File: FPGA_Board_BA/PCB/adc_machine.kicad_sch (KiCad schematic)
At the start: 6 parts, among them J201 PinHeader_03_male, U201 LTC2320-16_LVDS

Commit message: some schematic changes + Misc
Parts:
- removed C201, C202, C203, C204: 10u_1210, WLIB_Capacitor:C_1210, symbol WLIB_C:10u_1210
- removed J201: PinHeader_03_male, Connector_PinHeader_2.54mm:PinHeader_1x03_P2.54mm_Vertical, symbol WLIB_J:PinHeader_03_male
- removed U201: LTC2320-16_LVDS, MYLIB_chips:UKG_52_7mm_8mm, symbol MYLIB_U:LTC2320-16_LVDS
- added C1301, C1302, C1303, C1304: 10u_1210, WLIB_Capacitor:C_1210, symbol WLIB_C:10u_1210
- added U1301: LTC2320-16_LVDS, MYLIB_chips:UKG_52_7mm_8mm, symbol MYLIB_U:LTC2320-16_LVDS
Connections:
- net +5VA: now also U1301.15 (VDD), U1301.21 (VDD), U1301.43 (REFBUFEN), U1301.44 (VDD), U1301.52 (VDD)
- net GND: now also C1301.2, C1302.2, C1303.2, C1304.2, U1301.12 (GND), U1301.18 (GND), U1301.26 (GND), U1301.3 (GND), U1301.32 (GND), U1301.34 (CLKOUT-), U1301.38 (GND), U1301.46 (GND), U1301.49 (GND), U1301.53 (GND), U1301.7 (GND)
- net OVDD: now also U1301.23 (~{SDR}/DDR), U1301.25 (~{CMOS}/LVDS), U1301.31 (OVDD), U1301.37 (OVDD)
- new net: C1303.1, U1301.6 (REFOUT3)
- new net: C1301.1, U1301.22 (REFOUT1)
- new net: C1302.1, U1301.9 (REFOUT2)
- new net: C1304.1, U1301.45 (REFOUT4)
- new net CLK_IN_1: U1301.41 (SCK+)
- new net CLK_OUT_1: U1301.33 (CLKOUT+)
- new net SDO1_1: U1301.27 (SDOA+)
- new net SDO2_1: U1301.28 (SDOA-)
- new net SDO3_1: U1301.29 (SDOB+)
- new net SDO4_1: U1301.30 (SDOB-)
- new net SDO5_1: U1301.35 (SDOC+)
- new net SDO6_1: U1301.36 (SDOC-)
- new net SDO7_1: U1301.39 (SDOD+)
- new net SDO8_1: U1301.40 (SDOD-)
- new net ~{CNV}_1: U1301.24 (~{CNV})
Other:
- note removed: "Buffer for input: LT1819 or Leo circuit Not pseudo-differential!"
- note removed: "PinHeader for decide 1-2: SDR 2-3: DDR"

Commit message: lot of work
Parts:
- added J1301: PinHeader_03_male, Connector_PinHeader_2.54mm:PinHeader_1x03_P2.54mm_Vertical, symbol WLIB_J:PinHeader_03_male
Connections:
- net GND: now also J1301.1 (Pin_1)
- net Diffamp4/Ain-: now reaches U1301.10 (Ain4-)
- net Diffamp4/Ain+: now reaches U1301.11 (Ain4+)
- net Diffamp3/Ain-: now reaches U1301.13 (Ain3-)
- net Diffamp3/Ain+: now reaches U1301.14 (Ain3+)
- net Diffamp2/Ain-: now reaches U1301.16 (Ain2-)
- net Diffamp2/Ain+: now reaches U1301.17 (Ain2+)
- net Diffamp1/Ain-: now reaches U1301.19 (Ain1-)
- net Diffamp1/Ain+: now reaches U1301.20 (Ain1+)
- net OVDD: no longer names the net of U1301.23 (~{SDR}/DDR), U1301.25 (~{CMOS}/LVDS)
- net OVDD: now also J1301.2 (Pin_2); no longer U1301.31 (OVDD), U1301.37 (OVDD)
- new net +1V8: J1301.3 (Pin_3), U1301.31 (OVDD), U1301.37 (OVDD)
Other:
- added sheet Diffamp1 (diffamp_adc.kicad_sch)
- added sheet Diffamp2 (diffamp_adc.kicad_sch)
- added sheet Diffamp3 (diffamp_adc.kicad_sch)
- added sheet Diffamp4 (diffamp_adc.kicad_sch)
- added sheet Diffamp5 (diffamp_adc.kicad_sch)
- added sheet Diffamp6 (diffamp_adc.kicad_sch)
- added sheet Diffamp7 (diffamp_adc.kicad_sch)
- added sheet Diffamp8 (diffamp_adc.kicad_sch)
- note added: "PinHeader for decide 1-2: SDR 2-3: DDR"
- moved on the sheet: C1301, C1302, C1303, C1304, U1301

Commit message: work
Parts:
- removed U1301: LTC2320-16_LVDS, MYLIB_chips:UKG_52_7mm_8mm, symbol MYLIB_U:LTC2320-16_LVDS
- added C57, C58, C67: 1u_0603, WLIB_Capacitor:C_0603, symbol WLIB_C:1u_0603
- added C59, C60, C61, C62, C63, C64, C65, C66: 100n_0603, WLIB_Capacitor:C_0603, symbol WLIB_C:100n_0603
- added Q6: NTR5103NT1G, Package_TO_SOT_SMD:SOT-23_Handsoldering, symbol WLIB_Q:NTR5103NT1G
- added R52: 100R_0603, Resistor_SMD:R_0603_1608Metric, symbol WLIB_R:100R_0603
- added R53, R54: 10k_0603, Resistor_SMD:R_0603_1608Metric, symbol WLIB_R:10k_0603
- added U15: LTC2320-16_CMOS, MYLIB_chips:UKG_52_7mm_8mm, symbol MYLIB_U:LTC2320-16_CMOS
- renumbered C1301 to C68, C1302 to C69, C1303 to C70, C1304 to C71, J1301 to J19
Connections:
- net +1V8: now also C58.1, C60.1, C62.1, C64.1, C66.1, R54.1, U15.31 (OVDD), U15.37 (OVDD)
- net +5VA: now also C57.1, C59.1, C61.1, C63.1, C65.1, U15.15 (VDD), U15.21 (VDD), U15.43 (REFBUFEN), U15.44 (VDD), U15.52 (VDD)
- net CLK_IN_1: now also U15.41 (SCK)
- net CLK_OUT_1: now also U15.33 (CLKOUT+)
- net Diffamp1/Ain+: now also U15.20 (Ain1+)
- net Diffamp1/Ain-: now also U15.19 (Ain1-)
- net Diffamp2/Ain+: now also U15.17 (Ain2+)
- net Diffamp2/Ain-: now also U15.16 (Ain2-)
- net Diffamp3/Ain+: now also U15.14 (Ain3+)
- net Diffamp3/Ain-: now also U15.13 (Ain3-)
- net Diffamp4/Ain+: now also U15.11 (Ain4+)
- net Diffamp4/Ain-: now also U15.10 (Ain4-)
- net GND: now also C57.2, C58.2, C59.2, C60.2, C61.2, C62.2, C63.2, C64.2, C65.2, C66.2, C67.2, Q6.2 (S), R53.2, U15.12 (GND), U15.18 (GND), U15.25 (~{CMOS}/LVDS), U15.26 (GND), U15.3 (GND), U15.32 (GND), U15.34 (CLKOUT-), U15.38 (GND), U15.46 (GND), U15.49 (GND), U15.53 (GND), U15.7 (GND)
- net SDO1_1: now also U15.27 (SDO1)
- net SDO2_1: now also U15.28 (SDO2)
- net SDO3_1: now also U15.29 (SDO3)
- net SDO4_1: now also U15.30 (SDO4)
- net SDO5_1: now also U15.35 (SDO5)
- net SDO6_1: now also U15.36 (SDO6)
- net SDO7_1: now also U15.39 (SDO7)
- net SDO8_1: now also U15.40 (SDO8)
- net at C70.1: now also U15.6 (REFOUT3)
- net at C68.1: now also U15.22 (REFOUT1)
- net at C69.1: now also U15.9 (REFOUT2)
- net at J19.2 (Pin_2): now also U15.23 (~{SDR}/DDR)
- net at C71.1: now also U15.45 (REFOUT4)
- new net: Q6.1 (G), R52.2, R53.1
- new net: C67.1, U15.8 (REF)
- new net CNV_1: R52.1
- new net ~{CNV}: Q6.3 (D), R54.2, U15.24 (~{CNV})
- no-connect marks 1 -> 0
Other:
- moved on the sheet: C68, C69, C70, C71, J19

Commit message: 18.11 Bib Session
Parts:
- removed Q6: NTR5103NT1G, Package_TO_SOT_SMD:SOT-23_Handsoldering, symbol WLIB_Q:NTR5103NT1G
- removed R52: 100R_0603, Resistor_SMD:R_0603_1608Metric, symbol WLIB_R:100R_0603
- removed R53, R54: 10k_0603, Resistor_SMD:R_0603_1608Metric, symbol WLIB_R:10k_0603
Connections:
- net CLK_IN_1: no longer U15.41 (SCK)
- net ~{CNV} renamed Level Shift for DIO/B2
- new net Level Shift for DIO/B1: U15.41 (SCK)
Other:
- added sheet Level Shift for DIO (ls_for_dio.kicad_sch)

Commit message: 22.11
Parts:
- renumbered C57 to C58, C58 to C59, C59 to C60, C60 to C61, C61 to C62, C62 to C63, C63 to C64, C64 to C65, C65 to C66, C66 to C67, C67 to C68, C68 to C69, C69 to C70, C70 to C71, C71 to C72, U15 to U11
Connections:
- net Diffamp5/Ain+: now also U11.5 (Ain5+)
- net Diffamp5/Ain-: now also U11.4 (Ain5-)
- net Diffamp6/Ain+: now also U11.2 (Ain6+)
- net Diffamp6/Ain-: now also U11.1 (Ain6-)
- net Diffamp7/Ain+: now also U11.51 (Ain7+)
- net Diffamp7/Ain-: now also U11.50 (Ain7-)
- net Diffamp8/Ain+: now also U11.48 (Ain8+)
- net Diffamp8/Ain-: now also U11.47 (Ain8-)
- net REFOUT_1: now reaches C68.1, U11.8 (REF)

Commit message: exported stuff
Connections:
- net REFOUT_1 renamed REFOUT_M
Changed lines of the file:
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@@
+		)
+	)
+	(global_label "REFOUT_M"
+		(shape bidirectional)
+		(at 107.95 114.3 180)
+		(fields_autoplaced yes)
+		(effects
+			(font
+				(size 1.27 1.27)
+			)
+			(justify right)
+		)
+		(property "Intersheetrefs" "${INTERSHEET_REFS}"
+			(at 94.2983 114.3 0)
+			(effects
+				(font
+					(size 1.27 1.27)
+				)
+				(justify right)
+				(hide yes)
+			)
 		)
 	)
@@
 		(dnp no)
 		(fields_autoplaced yes)
-		(property "Reference" "#PWR086"
+		(property "Reference" "#PWR091"
 			(at 52.07 133.35 0)
 			(effects
@@
 			(project "FPGA_Board_BA"
 				(path "/fd7503bc-e7fc-4766-b224-3d1c3d7de5ff/61f82991-823e-4c29-9a78-9b2ec5b110b2"
-					(reference "#PWR086")
+					(reference "#PWR091")
 					(unit 1)
 				)
@@
 		(dnp no)
 		(fields_autoplaced yes)
-		(property "Reference" "#PWR093"
+		(property "Reference" "#PWR099"
 			(at 193.04 45.72 0)
 			(effects
@@
 			(project "FPGA_Board_BA"
 				(path "/fd7503bc-e7fc-4766-b224-3d1c3d7de5ff/61f82991-823e-4c29-9a78-9b2ec5b110b2"
-					(reference "#PWR093")
+					(reference "#PWR099")
 					(unit 1)
 				)
@@
 		(dnp no)
 		(fields_autoplaced yes)
-		(property "Reference" "#PWR087"
+		(property "Reference" "#PWR092"
 			(at 54.61 148.59 0)
 			(effects
@@
 			(project "FPGA_Board_BA"
 				(path "/fd7503bc-e7fc-4766-b224-3d1c3d7de5ff/61f82991-823e-4c29-9a78-9b2ec5b110b2"
-					(reference "#PWR087")
+					(reference "#PWR092")
 					(unit 1)
 				)
@@
 		(dnp no)
 		(fields_autoplaced yes)
-		(property "Reference" "#PWR091"
+		(property "Reference" "#PWR097"
 			(at 182.88 45.72 0)
 			(effects
@@
 			(project ""
 				(path "/fd7503bc-e7fc-4766-b224-3d1c3d7de5ff/61f82991-823e-4c29-9a78-9b2ec5b110b2"
-					(reference "#PWR091")
+					(reference "#PWR097")
 					(unit 1)
 				)
@@
 		(dnp no)
 		(fields_autoplaced yes)
-		(property "Reference" "#PWR089"
+		(property "Reference" "#PWR095"
 			(at 134.62 55.88 0)
 			(effects
@@
 			(project "FPGA_Board_BA"
 				(path "/fd7503bc-e7fc-4766-b224-3d1c3d7de5ff/61f82991-823e-4c29-9a78-9b2ec5b110b2"
-					(reference "#PWR089")
+					(reference "#PWR095")
 					(unit 1)
 				)
@@
 		(dnp no)
 		(fields_autoplaced yes)
-		(property "Reference" "#PWR090"
+		(property "Reference" "#PWR096"
 			(at 140.97 148.59 0)
 			(effects
@@
 			(project "FPGA_Board_BA"
 				(path "/fd7503bc-e7fc-4766-b224-3d1c3d7de5ff/61f82991-823e-4c29-9a78-9b2ec5b110b2"
-					(reference "#PWR090")
+					(reference "#PWR096")
 					(unit 1)
 				)
@@
 		(dnp no)
 		(fields_autoplaced yes)
-		(property "Reference" "#PWR088"
+		(property "Reference" "#PWR093"
 			(at 54.61 168.91 0)
 			(effects
@@
 			(project "FPGA_Board_BA"
 				(path "/fd7503bc-e7fc-4766-b224-3d1c3d7de5ff/61f82991-823e-4c29-9a78-9b2ec5b110b2"
-					(reference "#PWR088")
+					(reference "#PWR093")
 					(unit 1)
 				)
@@
 		(dnp no)
 		(fields_autoplaced yes)
-		(property "Reference" "#PWR085"
+		(property "Reference" "#PWR090"
 			(at 52.07 111.76 0)
 			(effects
@@
 			(project "FPGA_Board_BA"
 				(path "/fd7503bc-e7fc-4766-b224-3d1c3d7de5ff/61f82991-823e-4c29-9a78-9b2ec5b110b2"
-					(reference "#PWR085")
+					(reference "#PWR090")
 					(unit 1)
 				)
@@
 	)
 	(symbol
-		(lib_id "power:+5V")
-		(at 107.95 114.3 90)
-		(unit 1)
-		(exclude_from_sim no)
-		(in_bom yes)
-		(on_board yes)
-		(dnp no)
-		(fields_autoplaced yes)
-		(property "Reference" "#PWR0297"
-			(at 111.76 114.3 0)
-			(effects
-				(font
-					(size 1.27 1.27)
-				)
-				(hide yes)
-			)
-		)
-		(property "Value" "REFOUT_1"
-			(at 104.14 114.2999 90)
-			(effects
-				(font
-					(size 1.27 1.27)
-				)
-				(justify left)
-			)
-		)
-		(property "Footprint" ""
-			(at 107.95 114.3 0)
-			(effects
-				(font
-					(size 1.27 1.27)
-				)
-				(hide yes)
-			)
-		)
-		(property "Datasheet" ""
-			(at 107.95 114.3 0)
-			(effects
-				(font
-					(size 1.27 1.27)
-				)
-				(hide yes)
-			)
-		)
-		(property "Description" "Power symbol creates a global label with name \"REFOUT_1\""
-			(at 107.95 114.3 0)
-			(effects
-				(font
-					(size 1.27 1.27)
-				)
-				(hide yes)
-			)
-		)
-		(pin "1"
-		)
-		(instances
-			(project "FPGA_Board_BA"
-				(path "/fd7503bc-e7fc-4766-b224-3d1c3d7de5ff/61f82991-823e-4c29-9a78-9b2ec5b110b2"
-					(reference "#PWR0297")
-					(unit 1)
-				)
-			)
-		)
-	)
-	(symbol
 		(lib_id "WLIB_C:10u_1210")
 		(at 156.21 129.54 0)
@@
 		(dnp no)
 		(fields_autoplaced yes)
-		(property "Reference" "#PWR092"
+		(property "Reference" "#PWR098"
 			(at 187.96 143.51 0)
 			(effects
@@
 			(project "FPGA_Board_BA"
 				(path "/fd7503bc-e7fc-4766-b224-3d1c3d7de5ff/61f82991-823e-4c29-9a78-9b2ec5b110b2"
-					(reference "#PWR092")
-					(unit 1)
-				)
+					(reference "#PWR098")
+					(unit 1)
+				)

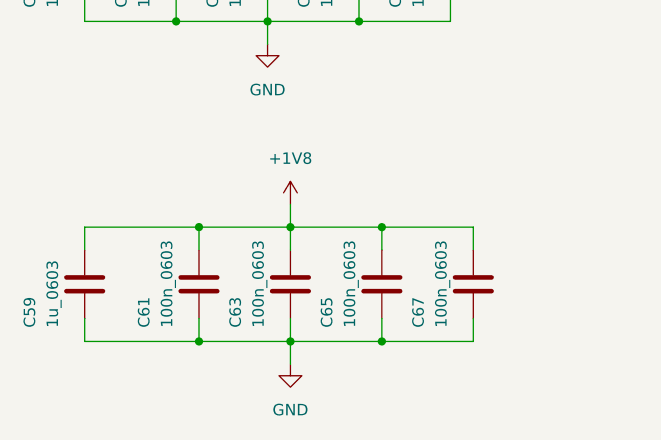
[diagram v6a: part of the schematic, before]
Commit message: layout of islands is ready
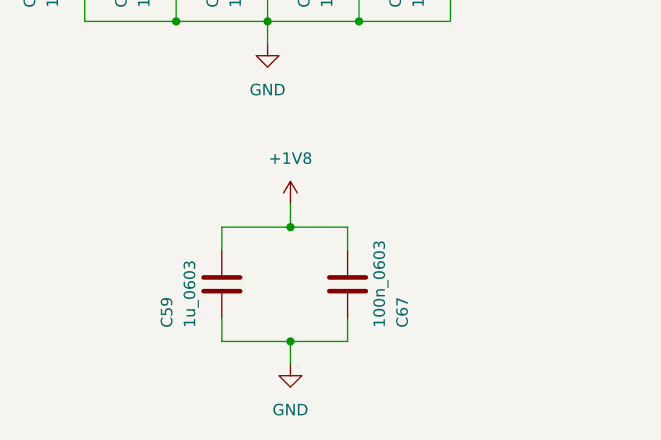
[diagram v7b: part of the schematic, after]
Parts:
- removed C61, C63, C65: 100n_0603, WLIB_Capacitor:C_0603, symbol WLIB_C:100n_0603
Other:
- moved on the sheet: C59, C67

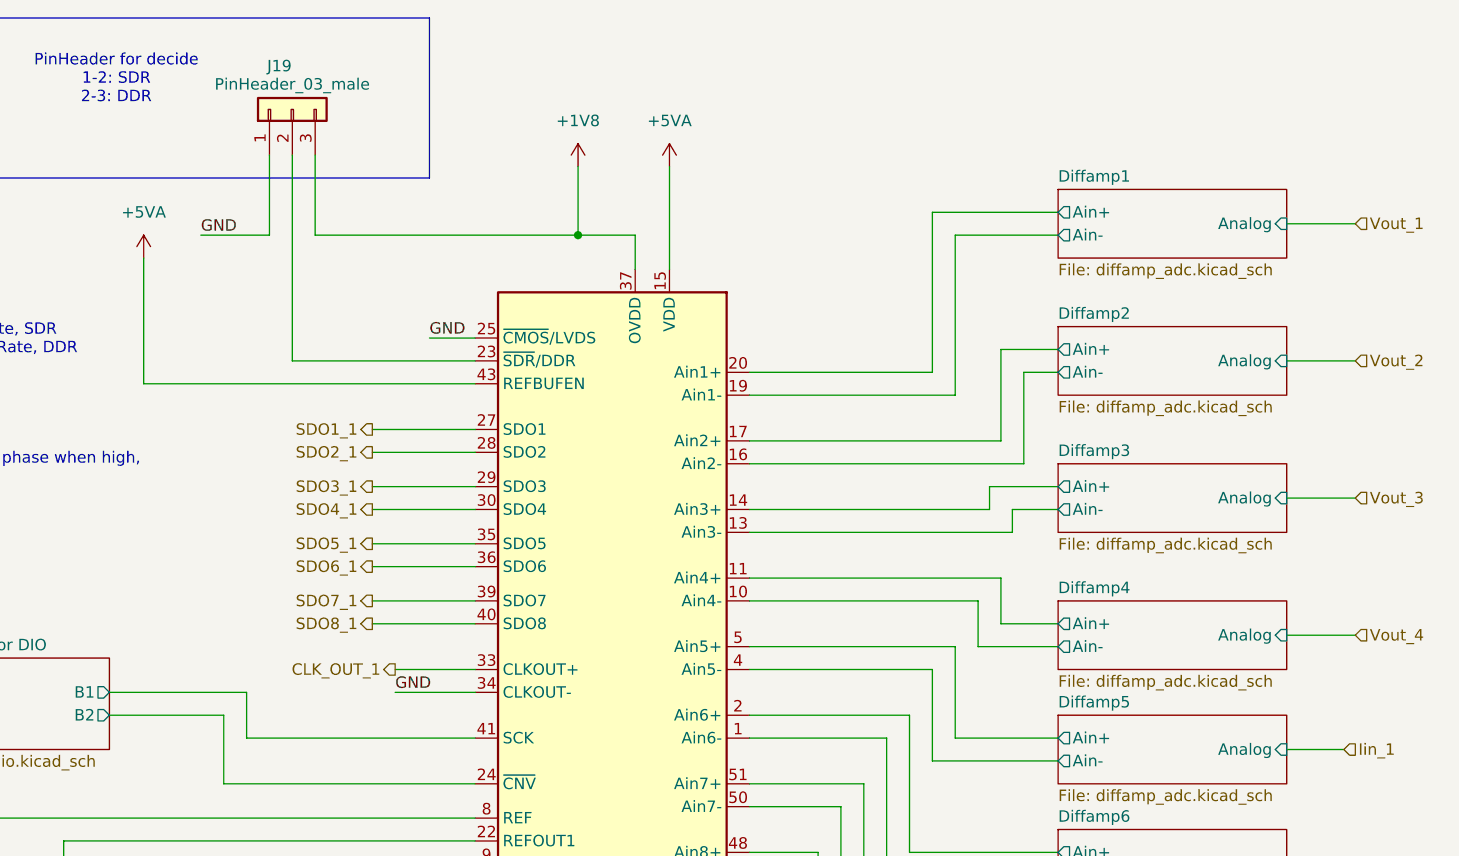
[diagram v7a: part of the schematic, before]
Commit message: component placement with new concept is ready
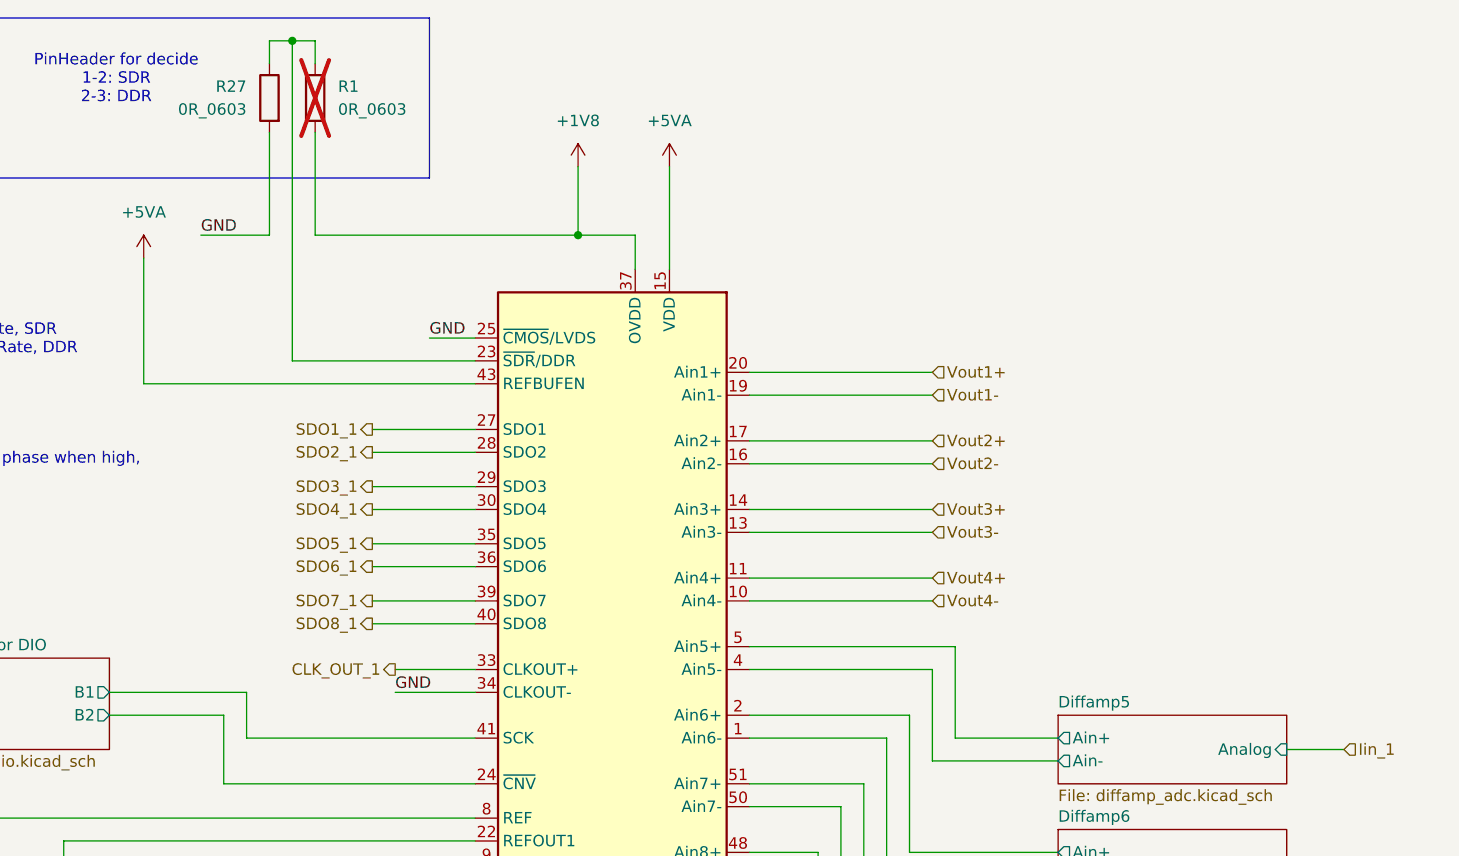
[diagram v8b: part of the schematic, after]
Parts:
- removed J19: PinHeader_03_male, Connector_PinHeader_2.54mm:PinHeader_1x03_P2.54mm_Vertical, symbol WLIB_J:PinHeader_03_male
- added R1, R27: 0R_0603, Resistor_SMD:R_0603_1608Metric, symbol WLIB_R:0R_0603
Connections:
- net +1V8: now also R1.2
- net GND: now also R27.2
- net at U11.23 (~{SDR}/DDR): now also R1.1, R27.1
- net Diffamp1/Ain+ renamed Vout1+
- net Diffamp1/Ain- renamed Vout1-
- net Diffamp2/Ain+ renamed Vout2+
- net Diffamp2/Ain- renamed Vout2-
- net Diffamp3/Ain+ renamed Vout3+
- net Diffamp3/Ain- renamed Vout3-
- net Diffamp4/Ain+ renamed Vout4+
- net Diffamp4/Ain- renamed Vout4-
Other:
- removed sheet Diffamp1
- removed sheet Diffamp2
- removed sheet Diffamp3
- removed sheet Diffamp4
